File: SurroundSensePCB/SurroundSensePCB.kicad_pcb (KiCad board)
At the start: 4 copper layers, 15.7 x 24.6 mm, 31 parts, among them J1 out_positive, J2 out_negative, J3 VIN, J4 GND_IN, U1 2.4GHz

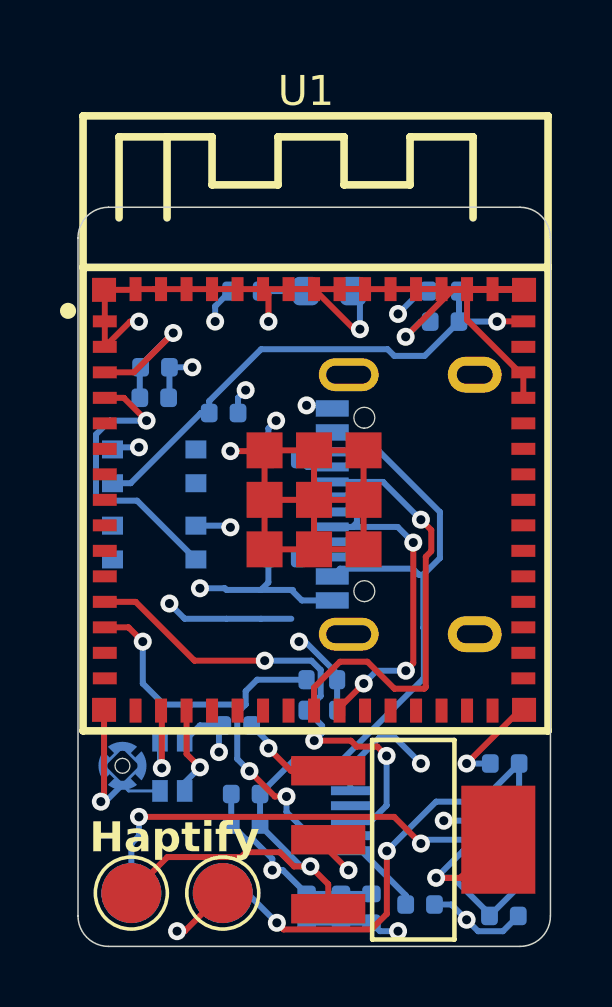
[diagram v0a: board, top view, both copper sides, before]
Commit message: parts selected, ordered
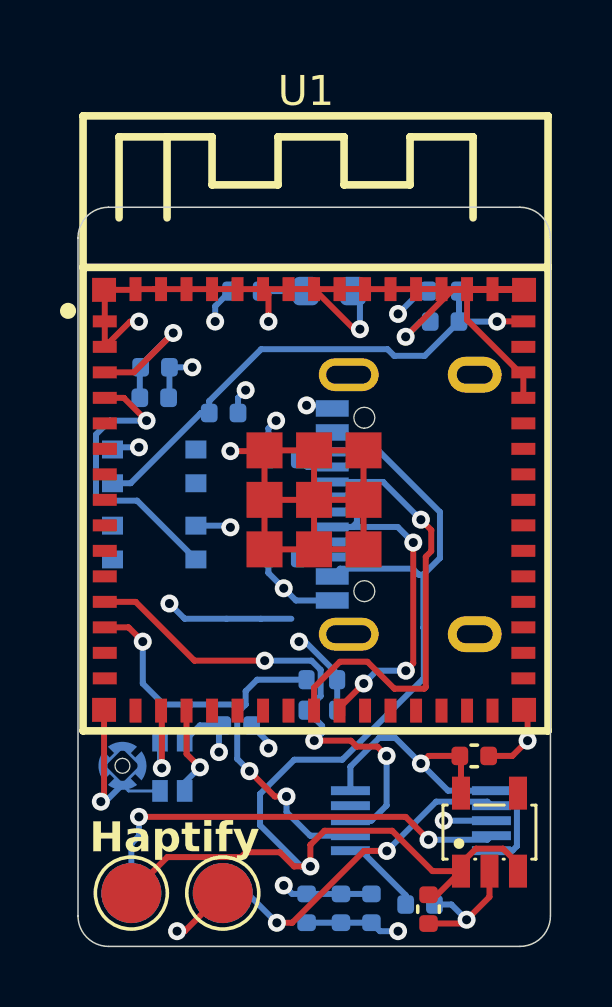
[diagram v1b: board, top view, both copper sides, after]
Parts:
- removed C12: 10uF, Capacitor_SMD:C_0402_1005Metric
- removed C13: 100nF, Capacitor_SMD:C_0402_1005Metric
- C10: value 10uF -> 1uF; moved to F.Cu
- C11: value 100nF -> 1uF; moved to F.Cu
- U3: footprint AMS1117-3.3:SOT-223-4_L6.5-W3.5-P2.30-LS7.0-BR -> TLV75533PDBVR:SOT-23-5_L3.0-W1.7-P0.95-LS2.8-BR
- moved U3 2.55 mm to (142.0, 97.3), turned to -90 degrees
- moved C10 2.52 mm to (140.0, 99.8), turned to 90 degrees
- moved C11 1.05 mm to (141.5, 94.7), turned to 0 degrees
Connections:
- C10 pad 1: +3.3V -> GND
- C10 pad 2: GND -> +5V
- U3 pad 1: GND -> +5V
- U3 pad 2: +3.3V -> GND
- U3 pad 4: +3.3V -> unconnected-(U3-NC-Pad4)
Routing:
- net +5V: track 32.4 -> 41.5 mm
- net GND: track 97.2 -> 88.5 mm
- net +3.3V: track 39.9 -> 33.6 mm, vias 10 -> 8
- net /out+: track 12.5 -> 11.1 mm
